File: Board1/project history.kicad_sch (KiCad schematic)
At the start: 0 parts

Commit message: v1.2 release of board with bug fixes etc
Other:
- note added: "5-Mar-2025 - Rev 1.2 Status: Prototype"
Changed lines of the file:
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@@
 (kicad_sch
-	(version 20231120)
+	(version 20250114)
 	(generator "eeschema")
-	(generator_version "8.0")
+	(generator_version "9.0")
 	(paper "A4")
 	(title_block
 		(title "Revision History")
-		(date "2025-02-19")
-		(rev "1.1")
+		(date "2025-03-08")
+		(rev "1.2")
 		(company "Wattle Labs")
+	)
+	(text "19-Feb-2025 - Rev 1.1\nStatus: Prototype"
+		(exclude_from_sim no)
+		(at 25.4 33.02 0)
+		(effects
+			(font
+				(size 2 2)
+				(thickness 0.25)
+				(color 0 0 0 1)
+			)
+			(justify left bottom)
+		)
+	)
+	(text "5-Mar-2025 - Rev 1.2\nStatus: Prototype"
+		(exclude_from_sim no)
+		(at 109.22 33.02 0)
+		(effects
+			(font
+				(size 2 2)
+				(thickness 0.25)
+				(color 0 0 0 1)
+			)
+			(justify left bottom)
+		)
+	)
+	(text "xx-xxx-20xx\nStatus: ???"
+		(exclude_from_sim no)
+		(at 198.12 33.02 0)
+		(effects
+			(font
+				(size 2 2)
+				(thickness 0.25)
+				(color 0 0 0 1)
+			)
+			(justify left bottom)
+		)
+	)
+	(text_box "* Removed LED for SSR indicator from board2 (and board1 pin header). It was found that this LED reduced the SSR outout and became impossible to get PTC plate to 200degC. Plan to implement a \"power meter\" bar graph in the OLED to show SSR drive.\n\n* Added InfraRed temperature sensor (MLX90614ESF) to board2 (and board1 pin header). This will read temperature from beneath the hot plate (and is somewhat of an experiement therefore the thermocouple driver remains on board).\n\n* Added ferrite beads to thermocouple inputs to reduce potential for EMI to upset temperature readings."
+		(exclude_from_sim no)
+		(at 25.4 38.1 0)
+		(size 76.2 154.94)
+		(margins 0.9524 0.9524 0.9524 0.9524)
+		(stroke
+			(width -0.0001)
+			(type default)
+		)
+		(fill
+			(type none)
+		)
+		(effects
+			(font
+				(size 1.27 1.27)
+				(color 0 0 0 1)
+			)
+			(justify left top)
+		)
+	)
+	(text_box "[${#}] ${TITLE}"
+		(exclude_from_sim no)
+		(at 12.065 12.065 0)
+		(size 273.05 13.335)
+		(margins 2.2499 2.2499 2.2499 2.2499)
+		(stroke
+			(width -0.0001)
+			(type default)
+		)
+		(fill
+			(type none)
+		)
+		(effects
+			(font
+				(size 3 3)
+				(thickness 0.375)
+			)
+		)
+	)
+	(text_box ""
+		(exclude_from_sim no)
+		(at 200.66 38.1 0)
+		(size 81.28 142.24)
+		(margins 0.9524 0.9524 0.9524 0.9524)
+		(stroke
+			(width -0.0001)
+			(type default)
+		)
+		(fill
+			(type none)
+		)
+		(effects
+			(font
+				(size 1.27 1.27)
+				(color 0 0 0 1)
+			)
+			(justify left top)
+		)
+	)
+	(text_box "* Migrate to KiCad 9.\n\n* Resolved ERC warnings on schematic and PCB.\n\n* Fixed missing ground connection for Reset switch.\n\n* Updated font size on pin header labels (JLCPCB was unable to print them at 1x1mm).\n\n* Updated bulk capacitor for the ESP32 module from 10u to 22u 16V (following Espressif best practise). Previous 10u cap had the board not booting reliably due to brownout.\n\n* Updated SSR to a zero crossing type to suit the PTCs resistive load.\n\n* Removed MAX31855 thermocouple chip and associated components. In practise the infrared thermometer performs better.\n\n* Updated FAN MOSFET drive circuit with a DGD0280WT MOSFET driver IC."
+		(exclude_from_sim no)
+		(at 109.22 38.1 0)
+		(size 81.28 142.24)
+		(margins 0.9524 0.9524 0.9524 0.9524)
+		(stroke
+			(width -0.0001)
+			(type solid)
+		)
+		(fill
+			(type none)
+		)
+		(effects
+			(font
+				(size 1.27 1.27)
+				(color 0 0 0 1)
+			)
+			(justify left top)
+		)
 	)
 	(polyline
@@
 		)
 	)
-	(text_box "* Removed LED for SSR indicator from board2 (and board1 pin header). It was found that this LED reduced the SSR outout and became impossible to get PTC plate to 200degC. Plan to implement a \"power meter\" bar graph in the OLED to show SSR drive.\n\n* Added InfraRed temperature sensor (MLX90614ESF) to board2 (and board1 pin header). This will read temperature from beneath the hot plate (and is somewhat of an experiement therefore the thermocouple driver remains on board).\n\n* Added ferrite beads to thermocouple inputs to reduce potential for EMI to upset temperature readings."
-		(exclude_from_sim no)
-		(at 25.4 38.1 0)
-		(size 76.2 154.94)
-		(stroke
-			(width -0.0001)
-			(type default)
-		)
-		(fill
-			(type none)
-		)
-		(effects
-			(font
-				(size 1.27 1.27)
-				(color 0 0 0 1)
-			)
-			(justify left top)
-		)
-	)
-	(text_box "[${#}] ${TITLE}"
-		(exclude_from_sim no)
-		(at 12.065 12.065 0)
-		(size 273.05 13.335)
-		(stroke
-			(width -0.0001)
-			(type default)
-		)
-		(fill
-			(type none)
-		)
-		(effects
-			(font
-				(size 3 3)
-				(thickness 0.375)
-			)
-		)
-	)
-	(text_box ""
-		(exclude_from_sim no)
-		(at 200.66 38.1 0)
-		(size 81.28 142.24)
-		(stroke
-			(width -0.0001)
-			(type default)
-		)
-		(fill
-			(type none)
-		)
-		(effects
-			(font
-				(size 1.27 1.27)
-				(color 0 0 0 1)
-			)
-			(justify left top)
-		)
-	)
-	(text_box ""
-		(exclude_from_sim no)
-		(at 109.22 38.1 0)
-		(size 81.28 142.24)
-		(stroke
-			(width -0.0001)
-			(type default)
-		)
-		(fill
-			(type none)
-		)
-		(effects
-			(font
-				(size 1.27 1.27)
-				(color 0 0 0 1)
-			)
-			(justify left top)
-		)
-	)
-	(text "19-Feb-2025 - Rev 1.1\nStatus: Prototype"
-		(exclude_from_sim no)
-		(at 25.4 33.02 0)
-		(effects
-			(font
-				(size 2 2)
-				(thickness 0.25)
-				(color 0 0 0 1)
-			)
-			(justify left bottom)
-		)
-	)
-	(text "xx-xxx-20xx\nStatus: ???"
-		(exclude_from_sim no)
-		(at 109.22 33.02 0)
-		(effects
-			(font
-				(size 2 2)
-				(thickness 0.25)
-				(color 0 0 0 1)
-			)
-			(justify left bottom)
-		)
-	)
-	(text "xx-xxx-20xx\nStatus: ???"
-		(exclude_from_sim no)
-		(at 198.12 33.02 0)
-		(effects
-			(font
-				(size 2 2)
-				(thickness 0.25)
-				(color 0 0 0 1)
-			)
-			(justify left bottom)
-		)
-	)

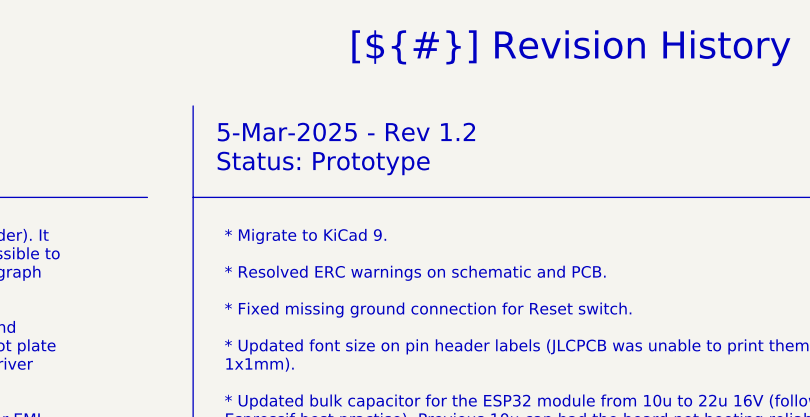
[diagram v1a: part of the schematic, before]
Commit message: Tweaks to schematic for clarity and minor firmware
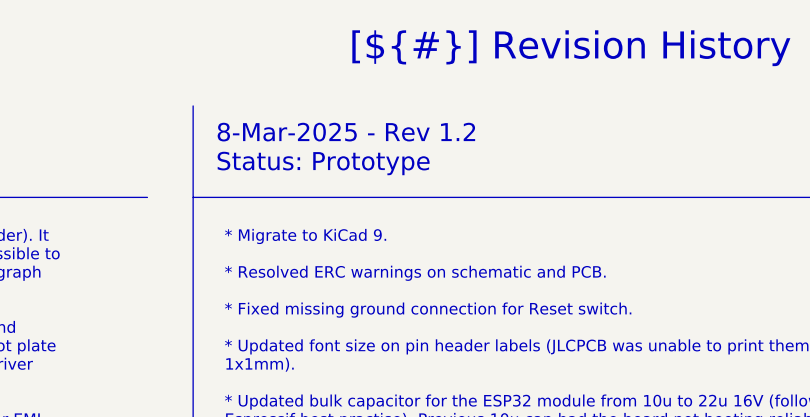
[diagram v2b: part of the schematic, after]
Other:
- note added: "8-Mar-2025 - Rev 1.2 Status: Prototype"
- note removed: "5-Mar-2025 - Rev 1.2 Status: Prototype"
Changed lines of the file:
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@@
 	(title_block
 		(title "Revision History")
-		(date "2025-03-08")
+		(date "2025-03-10")
 		(rev "1.2")
 		(company "Wattle Labs")
@@
 		)
 	)
-	(text "5-Mar-2025 - Rev 1.2\nStatus: Prototype"
+	(text "8-Mar-2025 - Rev 1.2\nStatus: Prototype"
 		(exclude_from_sim no)
 		(at 109.22 33.02 0)
